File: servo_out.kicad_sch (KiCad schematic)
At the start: 2 parts, among them M5 Motor_Servo_JR, Q17 AO3401A

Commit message: routing of H bridges and servo power pins
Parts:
- M5: footprint (none) -> Connector_PinHeader_2.54mm:PinHeader_1x03_P2.54mm_Horizontal
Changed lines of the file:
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@@
       (effects (font (size 1.27 1.27)) (justify left))
     )
-    (property "Footprint" "" (at 121.92 111.506 0)
+    (property "Footprint" "Connector_PinHeader_2.54mm:PinHeader_1x03_P2.54mm_Horizontal" (at 121.92 111.506 0)
       (effects (font (size 1.27 1.27)) hide)
     )

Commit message: jlcpcb part numbs
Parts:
- M5: JLCPCB Part# (none) -> C2935909
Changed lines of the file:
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@@
+      (effects (font (size 1.27 1.27)) hide)
+    )
+    (property "JLCPCB Part#" "C2935909" (at 121.92 106.68 0)
       (effects (font (size 1.27 1.27)) hide)
     )

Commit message: added moany componaets
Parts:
- M5: footprint Connector_PinHeader_2.54mm:PinHeader_1x03_P2.54mm_Horizontal -> Connector_PinHeader_2.54mm:PinHeader_1x03_P2.54mm_Vertical
- Q17: JLCPCB Part# (none) -> C15127
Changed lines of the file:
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@@
       (effects (font (size 1.27 1.27)) (justify left) hide)
+    )
+    (property "JLCPCB Part#" "C15127" (at 106.045 96.52 0)
+      (effects (font (size 1.27 1.27)) hide)
     )
     (pin "1")
@@
       (effects (font (size 1.27 1.27)) (justify left))
     )
-    (property "Footprint" "Connector_PinHeader_2.54mm:PinHeader_1x03_P2.54mm_Horizontal" (at 121.92 111.506 0)
+    (property "Footprint" "Connector_PinHeader_2.54mm:PinHeader_1x03_P2.54mm_Vertical" (at 121.92 111.506 0)
       (effects (font (size 1.27 1.27)) hide)
     )

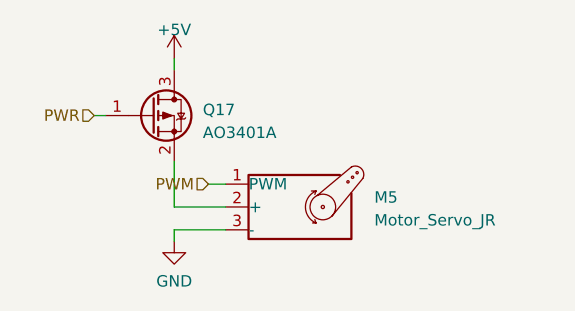
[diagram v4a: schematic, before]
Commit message: specified correct shift register
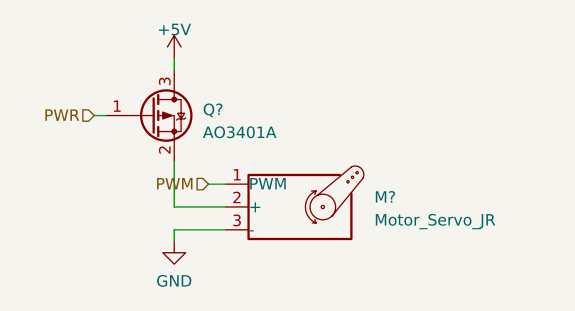
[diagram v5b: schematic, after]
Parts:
- renumbered M5 to M?, Q17 to Q?
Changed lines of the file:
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@@
   (symbol (lib_id "power:GND") (at 108.585 110.49 0) (unit 1)
     (in_bom yes) (on_board yes) (dnp no) (fields_autoplaced)
-    (property "Reference" "#PWR038" (at 108.585 116.84 0)
+    (property "Reference" "#PWR?" (at 108.585 116.84 0)
       (effects (font (size 1.27 1.27)) hide)
     )
@@
       (project "version_1"
         (path "/23ba0750-4a55-4d50-828b-749cc0fbb8c8"
-          (reference "#PWR038") (unit 1)
+          (reference "#PWR?") (unit 1)
         )
         (path "/23ba0750-4a55-4d50-828b-749cc0fbb8c8/9cb149a2-fbaf-4e99-919f-0fea623a18aa"
@@
   (symbol (lib_id "power:+5V") (at 108.585 90.17 0) (unit 1)
     (in_bom yes) (on_board yes) (dnp no) (fields_autoplaced)
-    (property "Reference" "#PWR035" (at 108.585 93.98 0)
+    (property "Reference" "#PWR?" (at 108.585 93.98 0)
       (effects (font (size 1.27 1.27)) hide)
     )
@@
       (project "version_1"
         (path "/23ba0750-4a55-4d50-828b-749cc0fbb8c8"
-          (reference "#PWR035") (unit 1)
+          (reference "#PWR?") (unit 1)
         )
         (path "/23ba0750-4a55-4d50-828b-749cc0fbb8c8/9cb149a2-fbaf-4e99-919f-0fea623a18aa"
@@
   (symbol (lib_id "Transistor_FET:AO3401A") (at 106.045 96.52 0) (unit 1)
     (in_bom yes) (on_board yes) (dnp no) (fields_autoplaced)
-    (property "Reference" "Q17" (at 111.76 95.885 0)
+    (property "Reference" "Q?" (at 111.76 95.885 0)
       (effects (font (size 1.27 1.27)) (justify left))
     )
@@
       (project "version_1"
         (path "/23ba0750-4a55-4d50-828b-749cc0fbb8c8"
-          (reference "Q17") (unit 1)
+          (reference "Q?") (unit 1)
         )
         (path "/23ba0750-4a55-4d50-828b-749cc0fbb8c8/9cb149a2-fbaf-4e99-919f-0fea623a18aa"
@@
   (symbol (lib_id "Motor:Motor_Servo_JR") (at 121.92 106.68 0) (unit 1)
     (in_bom yes) (on_board yes) (dnp no) (fields_autoplaced)
-    (property "Reference" "M5" (at 130.81 105.6116 0)
+    (property "Reference" "M?" (at 130.81 105.6116 0)
       (effects (font (size 1.27 1.27)) (justify left))
     )
@@
       (project "version_1"
         (path "/23ba0750-4a55-4d50-828b-749cc0fbb8c8"
-          (reference "M5") (unit 1)
+          (reference "M?") (unit 1)
         )
         (path "/23ba0750-4a55-4d50-828b-749cc0fbb8c8/9cb149a2-fbaf-4e99-919f-0fea623a18aa"

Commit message: fliped servo mosfets
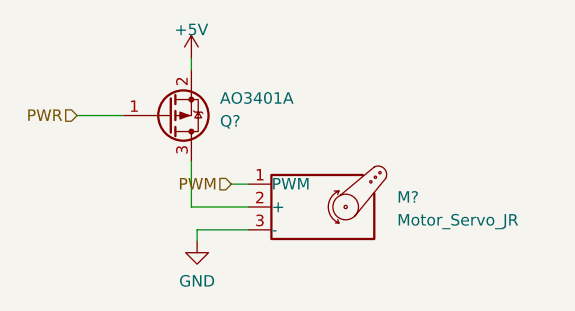
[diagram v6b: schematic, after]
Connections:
- net +5V: now also Q?.2 (S); no longer Q?.3 (D)
- net at M?.2 (+): now also Q?.3 (D); no longer Q?.2 (S)
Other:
- moved on the sheet: M?, Q?
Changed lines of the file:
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@@
 (kicad_sch (version 20230121) (generator eeschema)
   (paper "A4")
-  (wire (pts (xy 108.585 90.17) (xy 108.585 91.44))
+  (wire (pts (xy 97.79 96.52) (xy 102.87 96.52))
     (stroke (width 0) (type default))
   )
-  (wire (pts (xy 99.695 96.52) (xy 100.965 96.52))
+  (wire (pts (xy 111.125 109.22) (xy 116.84 109.22))
     (stroke (width 0) (type default))
   )
-  (wire (pts (xy 108.585 109.22) (xy 114.3 109.22))
+  (wire (pts (xy 110.49 101.6) (xy 110.49 106.68))
     (stroke (width 0) (type default))
   )
-  (wire (pts (xy 108.585 101.6) (xy 108.585 106.68))
+  (wire (pts (xy 110.49 90.17) (xy 110.49 91.44))
     (stroke (width 0) (type default))
   )
-  (wire (pts (xy 112.395 104.14) (xy 114.3 104.14))
+  (wire (pts (xy 114.935 104.14) (xy 116.84 104.14))
     (stroke (width 0) (type default))
   )
-  (wire (pts (xy 108.585 106.68) (xy 114.3 106.68))
+  (wire (pts (xy 110.49 106.68) (xy 116.84 106.68))
     (stroke (width 0) (type default))
   )
-  (wire (pts (xy 108.585 109.22) (xy 108.585 110.49))
+  (wire (pts (xy 111.125 109.22) (xy 111.125 110.49))
     (stroke (width 0) (type default))
   )
-  (hierarchical_label "PWR" (shape input) (at 99.695 96.52 180) (fields_autoplaced)
+  (hierarchical_label "PWR" (shape input) (at 97.79 96.52 180) (fields_autoplaced)
     (effects (font (size 1.27 1.27)) (justify right))
   )
-  (hierarchical_label "PWM" (shape input) (at 112.395 104.14 180) (fields_autoplaced)
+  (hierarchical_label "PWM" (shape input) (at 114.935 104.14 180) (fields_autoplaced)
     (effects (font (size 1.27 1.27)) (justify right))
   )
-  (symbol (lib_id "power:GND") (at 108.585 110.49 0) (unit 1)
+  (symbol (lib_id "power:GND") (at 111.125 110.49 0) (unit 1)
     (in_bom yes) (on_board yes) (dnp no) (fields_autoplaced)
-    (property "Reference" "#PWR?" (at 108.585 116.84 0)
+    (property "Reference" "#PWR?" (at 111.125 116.84 0)
       (effects (font (size 1.27 1.27)) hide)
     )
-    (property "Value" "GND" (at 108.585 114.935 0)
+    (property "Value" "GND" (at 111.125 114.935 0)
       (effects (font (size 1.27 1.27)))
     )
-    (property "Footprint" "" (at 108.585 110.49 0)
+    (property "Footprint" "" (at 111.125 110.49 0)
       (effects (font (size 1.27 1.27)) hide)
     )
-    (property "Datasheet" "" (at 108.585 110.49 0)
+    (property "Datasheet" "" (at 111.125 110.49 0)
       (effects (font (size 1.27 1.27)) hide)
     )
@@
     )
   )
-  (symbol (lib_id "power:+5V") (at 108.585 90.17 0) (unit 1)
+  (symbol (lib_id "power:+5V") (at 110.49 90.17 0) (unit 1)
     (in_bom yes) (on_board yes) (dnp no) (fields_autoplaced)
-    (property "Reference" "#PWR?" (at 108.585 93.98 0)
+    (property "Reference" "#PWR?" (at 110.49 93.98 0)
       (effects (font (size 1.27 1.27)) hide)
     )
-    (property "Value" "+5V" (at 108.585 86.995 0)
+    (property "Value" "+5V" (at 110.49 86.995 0)
       (effects (font (size 1.27 1.27)))
     )
-    (property "Footprint" "" (at 108.585 90.17 0)
+    (property "Footprint" "" (at 110.49 90.17 0)
       (effects (font (size 1.27 1.27)) hide)
     )
-    (property "Datasheet" "" (at 108.585 90.17 0)
+    (property "Datasheet" "" (at 110.49 90.17 0)
       (effects (font (size 1.27 1.27)) hide)
     )
@@
     )
   )
-  (symbol (lib_id "Transistor_FET:AO3401A") (at 106.045 96.52 0) (unit 1)
+  (symbol (lib_id "Transistor_FET:AO3401A") (at 107.95 96.52 0) (mirror x) (unit 1)
     (in_bom yes) (on_board yes) (dnp no) (fields_autoplaced)
-    (property "Reference" "Q?" (at 111.76 95.885 0)
+    (property "Reference" "Q?" (at 113.665 97.155 0)
       (effects (font (size 1.27 1.27)) (justify left))
     )
-    (property "Value" "AO3401A" (at 111.76 98.425 0)
+    (property "Value" "AO3401A" (at 113.665 94.615 0)
       (effects (font (size 1.27 1.27)) (justify left))
     )
-    (property "Footprint" "Package_TO_SOT_SMD:SOT-23" (at 111.125 98.425 0)
+    (property "Footprint" "Package_TO_SOT_SMD:SOT-23" (at 113.03 94.615 0)
       (effects (font (size 1.27 1.27) italic) (justify left) hide)
     )
-    (property "Datasheet" "http://www.aosmd.com/pdfs/datasheet/AO3401A.pdf" (at 106.045 96.52 0)
+    (property "Datasheet" "http://www.aosmd.com/pdfs/datasheet/AO3401A.pdf" (at 107.95 96.52 0)
       (effects (font (size 1.27 1.27)) (justify left) hide)
     )
-    (property "JLCPCB Part#" "C15127" (at 106.045 96.52 0)
+    (property "JLCPCB Part#" "C15127" (at 107.95 96.52 0)
       (effects (font (size 1.27 1.27)) hide)
     )
@@
     )
   )
-  (symbol (lib_id "Motor:Motor_Servo_JR") (at 121.92 106.68 0) (unit 1)
+  (symbol (lib_id "Motor:Motor_Servo_JR") (at 124.46 106.68 0) (unit 1)
     (in_bom yes) (on_board yes) (dnp no) (fields_autoplaced)
-    (property "Reference" "M?" (at 130.81 105.6116 0)
+    (property "Reference" "M?" (at 133.35 105.6116 0)
       (effects (font (size 1.27 1.27)) (justify left))
     )
-    (property "Value" "Motor_Servo_JR" (at 130.81 108.1516 0)
+    (property "Value" "Motor_Servo_JR" (at 133.35 108.1516 0)
       (effects (font (size 1.27 1.27)) (justify left))
     )
-    (property "Footprint" "Connector_PinHeader_2.54mm:PinHeader_1x03_P2.54mm_Vertical" (at 121.92 111.506 0)
+    (property "Footprint" "Connector_PinHeader_2.54mm:PinHeader_1x03_P2.54mm_Vertical" (at 124.46 111.506 0)
       (effects (font (size 1.27 1.27)) hide)
     )
-    (property "Datasheet" "http://forums.parallax.com/uploads/attachments/46831/74481.png" (at 121.92 111.506 0)
+    (property "Datasheet" "http://forums.parallax.com/uploads/attachments/46831/74481.png" (at 124.46 111.506 0)
       (effects (font (size 1.27 1.27)) hide)
     )
-    (property "JLCPCB Part#" "C2935909" (at 121.92 106.68 0)
+    (property "JLCPCB Part#" "C2935909" (at 124.46 106.68 0)
       (effects (font (size 1.27 1.27)) hide)
     )
